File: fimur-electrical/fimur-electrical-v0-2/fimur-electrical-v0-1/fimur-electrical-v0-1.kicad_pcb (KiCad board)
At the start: 2 copper layers, 37 x 25 mm, 18 parts, among them J1 Conn_01x04_Pin, J2 Conn_01x04_Pin, J3 Conn_02x03_Odd_Even, U1 NCP163AFCS180T2G, U2 ICM-20948, U3 ICM-20948

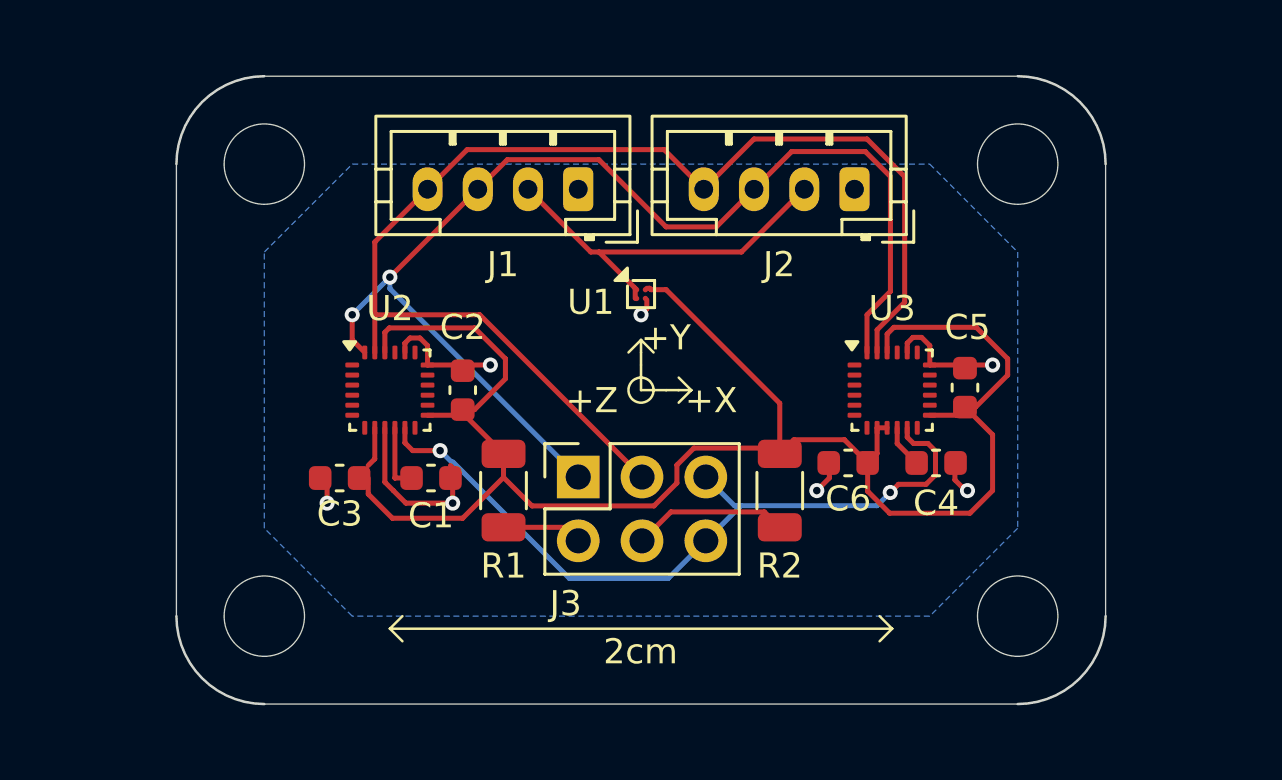
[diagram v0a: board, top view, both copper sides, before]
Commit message: multiplex schematic and layout and standardization with 2-imu board
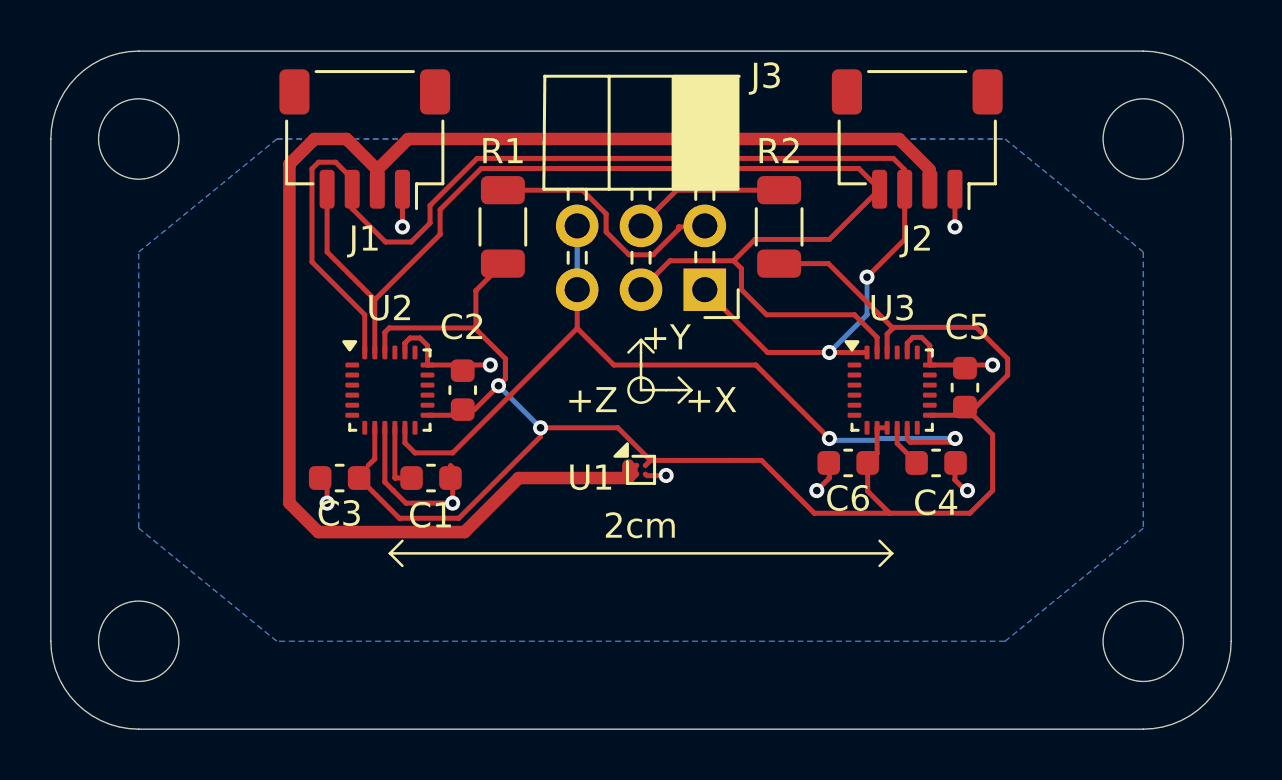
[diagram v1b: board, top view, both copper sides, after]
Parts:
- J1, J2: footprint Connector_JST:JST_PH_B4B-PH-K_1x04_P2.00mm_Vertical -> Connector_JST:JST_SH_SM04B-SRSS-TB_1x04-1MP_P1.00mm_Horizontal
- J3: footprint Connector_PinSocket_2.54mm:PinSocket_2x03_P2.54mm_Vertical -> Connector_PinSocket_2.54mm:PinSocket_2x03_P2.54mm_Horizontal
- moved R1 10.5 mm to (94.5, 93.5), turned to 90 degrees
- moved R2 10.5 mm to (105.5, 93.5), turned to 90 degrees
- moved J3 9.00 mm to (102.5, 96.0), turned to -90 degrees
- moved J1 8.73 mm to (89.0, 90.0)
- moved U1 7.00 mm to (100.0, 103.2)
- moved REF** 5.10 mm to (120.0, 90.0)
- moved REF** 5.10 mm to (120.0, 110.0)
- moved REF** 5.10 mm to (80.0, 110.0)
- moved REF** 5.10 mm to (80.0, 90.0)
- moved J2 3.20 mm to (111.0, 90.0)
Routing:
- net Net-(J1-Pin_2): track 15.5 -> 58.9 mm
- net Net-(J3-Pin_2): track 3.20 -> 10.1 mm
- net Net-(J1-Pin_3): track 46.9 -> 52.4 mm
- net GND: track 20.3 -> 23.4 mm, vias 7 -> 9
- net Net-(J3-Pin_5): track 30.2 -> 33.2 mm
- net Net-(U1-VOUT): track 72.2 -> 71.3 mm, vias 0 -> 2
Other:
- board size 37 x 25 mm -> 47 x 27 mm

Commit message: cleanup of v10.1.1
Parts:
- added 1V8: TestPoint_Loop_D1.80mm_Drill1.0mm_Beaded, TestPoint:TestPoint_Loop_D1.80mm_Drill1.0mm_Beaded, F.Cu at (104.0, 103.0)
- added GND: TestPoint_Loop_D1.80mm_Drill1.0mm_Beaded, TestPoint:TestPoint_Loop_D1.80mm_Drill1.0mm_Beaded, F.Cu at (114.5, 95.0)
- added VCC: TestPoint_Loop_D1.80mm_Drill1.0mm_Beaded, TestPoint:TestPoint_Loop_D1.80mm_Drill1.0mm_Beaded, F.Cu at (86.0, 97.0)
- J3: value Conn_02x03_Odd_Even -> Conn_02x02_Odd_Even; footprint Connector_PinSocket_2.54mm:PinSocket_2x03_P2.54mm_Horizontal -> Connector_PinSocket_2.54mm:PinSocket_2x02_P2.54mm_Horizontal
- moved R1 10.1 mm to (104.5, 95.0)
- moved J3 2.59 mm to (100.0, 96.5)
- moved R2 2.12 mm to (107.0, 95.0)
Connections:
- C2 pad 1: Net-(U1-VOUT) -> Net-(J3-Pin_2)
- C3 pad 1: Net-(U1-VOUT) -> Net-(J3-Pin_2)
- C5 pad 1: Net-(U1-VOUT) -> Net-(J3-Pin_2)
- C6 pad 1: Net-(U1-VOUT) -> Net-(J3-Pin_2)
- J3 pad 1: Net-(J1-Pin_3) -> Net-(J3-Pin_1)
- J3 pad 3: Net-(J1-Pin_4) -> Net-(J3-Pin_3)
- J3 pad 4: Net-(J3-Pin_4) -> Net-(J3-Pin_3)
- R1 pad 1: Net-(U1-VOUT) -> Net-(J3-Pin_1)
- R1 pad 2: Net-(J3-Pin_2) -> Net-(J1-Pin_3)
- R2 pad 1: Net-(U1-VOUT) -> Net-(J3-Pin_1)
- R2 pad 2: Net-(J3-Pin_4) -> Net-(J1-Pin_4)
- U1 pad A2: Net-(U1-VOUT) -> Net-(J3-Pin_2)
- U2 pad 11: Net-(J3-Pin_5) -> Net-(J3-Pin_3)
- U2 pad 13: Net-(U1-VOUT) -> Net-(J3-Pin_2)
- U2 pad 22: Net-(U1-VOUT) -> Net-(J3-Pin_2)
- U2 pad 8: Net-(U1-VOUT) -> Net-(J3-Pin_2)
- U3 pad 11: Net-(J3-Pin_5) -> Net-(J3-Pin_3)
- U3 pad 13: Net-(U1-VOUT) -> Net-(J3-Pin_2)
- U3 pad 22: Net-(U1-VOUT) -> Net-(J3-Pin_2)
- U3 pad 8: Net-(U1-VOUT) -> Net-(J3-Pin_2)
- U3 pad 9: Net-(U1-VOUT) -> Net-(J3-Pin_2)
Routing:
- net Net-(U1-VOUT): track 71.3 -> 0.00 mm, vias 2 -> 0
- net Net-(J3-Pin_2): track 10.1 -> 74.9 mm, vias 0 -> 2
- net Net-(J3-Pin_5): track 33.2 -> 0.00 mm, vias 2 -> 0
- net Net-(J3-Pin_3): track 0.00 -> 32.7 mm, vias 0 -> 2
- net Net-(J3-Pin_1): track 0.00 -> 7.02 mm
- net Net-(J3-Pin_4): track 6.09 -> 0.00 mm
- net Net-(J1-Pin_4): track 49.7 -> 46.8 mm
- net GND: track 23.4 -> 25.8 mm, vias 9 -> 8
- net Net-(J1-Pin_3): track 52.4 -> 51.7 mm
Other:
- board text added: "1cm"
- board text added: "4cm"
- board text added: "FSYNC"
- board text added: "PULLUP"
- board text added: "VCC: 2.2 - 5.5V"
